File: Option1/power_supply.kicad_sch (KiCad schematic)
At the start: 25 parts, among them U201 U7812-500, U202 U7805-500, U203 SY8089AAAC

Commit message: Platine korrigeiert, 5V DCDC getauscht, 3.3V Display Versorgung entfernt. Bauteile neu angeordnet, USB 5V auf 5V Supply geführt
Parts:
- renumbered C1 to C205
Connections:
- net 48V: no longer C201.1, C204.1, D201.2 (K), U201.1 (Vin), U202.1 (Vin)
- net 5V: no longer C205.1, F203.1, U202.3 (Vout)
- new net: C205.1, F203.1, U202.3 (Vout)
- new net 48V_Fused: C201.1, C204.1, D201.2 (K), U201.1 (Vin), U202.1 (Vin)
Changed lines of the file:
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@@
 	)
 	(label "48V_FUSED"
-		(at 57.15 25.4 0)
+		(at 59.69 25.4 0)
 		(effects
 			(font
@@
 		)
 	)
-	(label "5V"
-		(at 60.96 77.47 0)
+	(label "48V_FUSED"
+		(at 33.02 77.47 0)
 		(effects
 			(font
@@
 		)
 	)
-	(label "48V"
-		(at 35.56 77.47 0)
+	(label "5V"
+		(at 81.28 77.47 0)
 		(effects
 			(font
@@
 		(on_board yes)
 		(dnp no)
-		(property "Reference" "C1"
+		(property "Reference" "C205"
 			(at 67.31 90.17 90)
 			(effects
@@
 			(project "Option1"
 				(path "/b9e5f262-9648-4b79-bdd1-af888b822329/ff0aab3a-6ec2-4a6b-b0bf-5e79396b738a"
-					(reference "C1")
+					(reference "C205")
 					(unit 1)
 				)

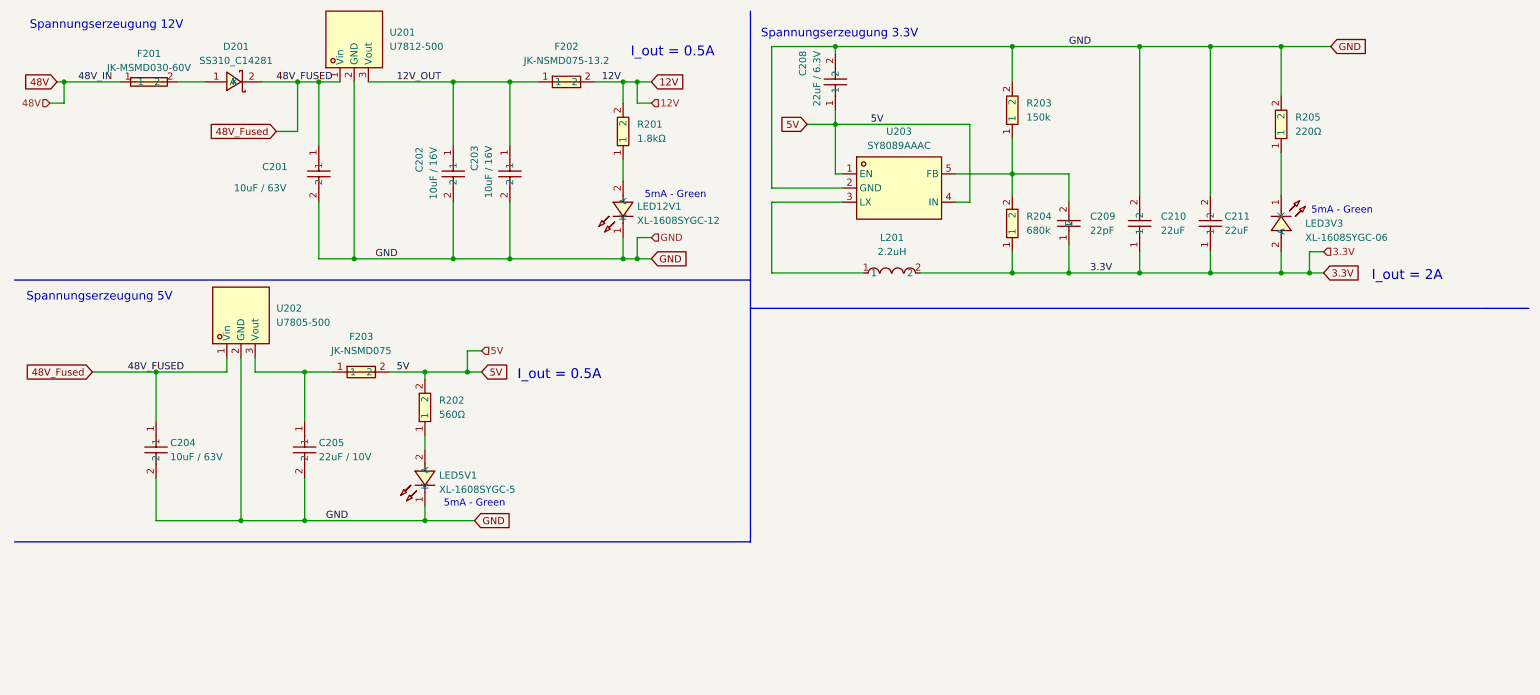
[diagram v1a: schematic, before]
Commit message: power Supply angepasst für 12V und 48V, Datenblätter für DCDCs hinzugefügt
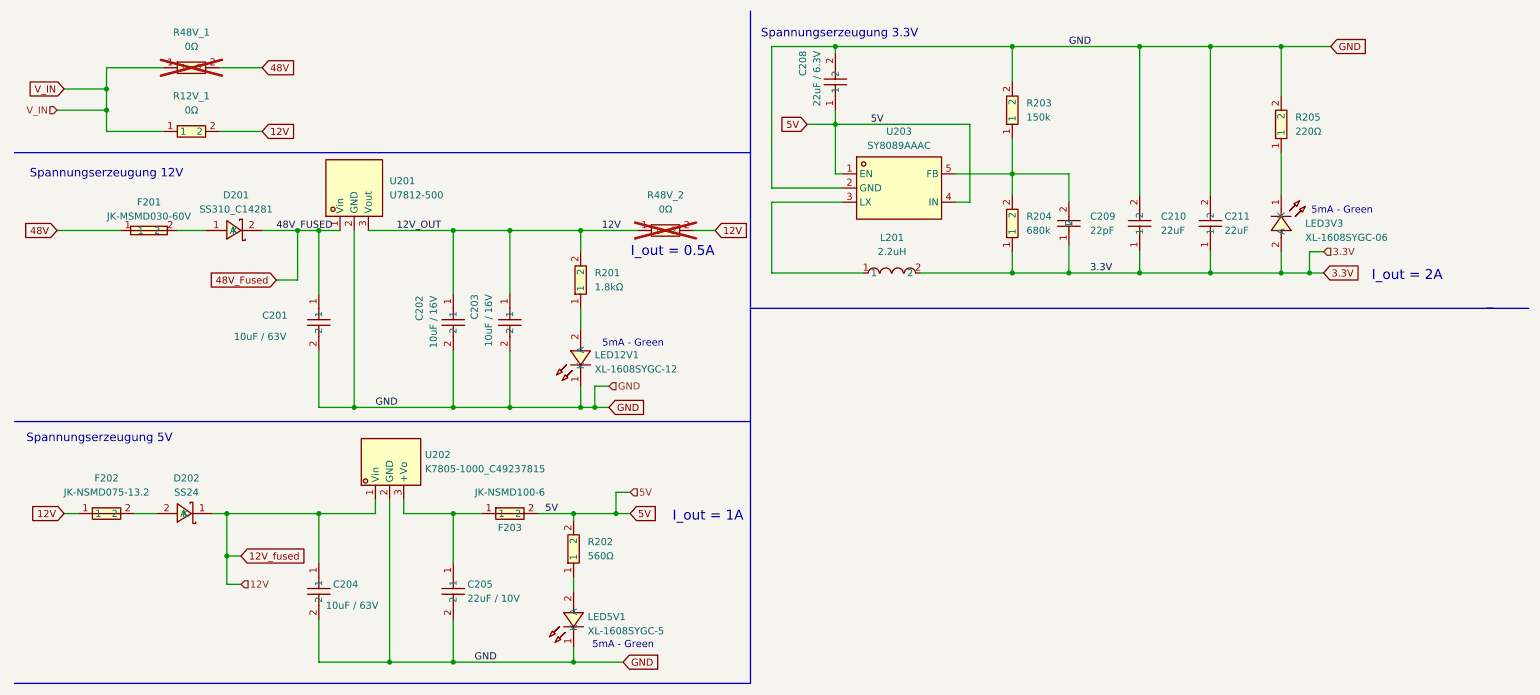
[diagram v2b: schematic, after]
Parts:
- removed F203: JK-NSMD075, easyeda2kicad:F1206, symbol easyeda2kicad:JK-NSMD075-13.2
- removed U202: U7805-500, easyeda2kicad:PWRM-TH_3P-L11.6-W9.0-P2.54, symbol easyeda2kicad:U7805-500
- added D202: SS24, easyeda2kicad:SMA_L4.3-W2.6-LS5.2-RD, symbol easyeda2kicad:SS24
- added F203: JK-NSMD100-6, easyeda2kicad:F1206, symbol easyeda2kicad:JK-NSMD100-6
- added R12V_1, R48V_1, R48V_2: 0Ω, easyeda2kicad:R0603, symbol easyeda2kicad:0603WAF0000T5E
- added U202: K7805-1000_C49237815, easyeda2kicad:PWRM-TH_K78XX-1000R, symbol easyeda2kicad:K7805-1000_C49237815
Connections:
- net 12V_OUT is gone; now on net 12V: C202.1, C203.1, F202.1, U201.3 (Vout)
- net 12V: now also C204.1, D202.1 (K), R12V_1.2, R48V_2.1, R48V_2.2, U202.1 (Vin); no longer F202.2
- net 48V: now also R48V_1.2
- net 48V_Fused: no longer C204.1
- net 5V: now also F203.2
- net GND: now also U202.2 (GND)
- net at C205.1: now also F203.1, U202.3 (+Vo)
- new net: D202.2 (A), F202.2
- new net V_IN: R12V_1.1, R48V_1.1
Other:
- note added: "I_out = 1A"
- moved on the sheet: C201, C202, C203, C204, C205, D201, F201, LED12V1, LED5V1, R201, R202, U201
